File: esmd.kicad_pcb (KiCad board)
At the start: 2 copper layers, 25.9 x 63 mm, 21 parts, among them J1 Conn_01x04, J2 Conn_01x08, J3 Conn_01x04, J4 Conn_01x08, J5 Conn_01x04, J6 Conn_01x08, J7 Conn_01x02, J8 Conn_01x02, U1 74HC245, U2 74HC245, U3 LM78M05_TO252

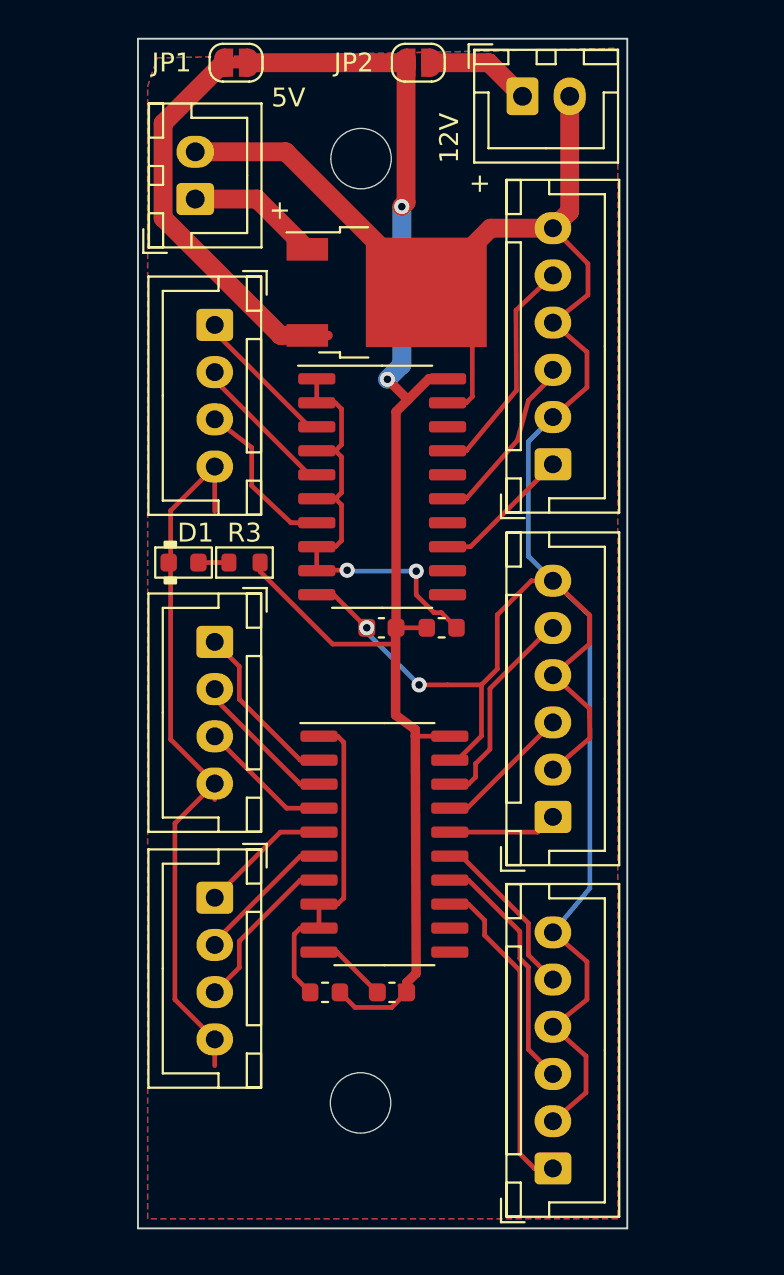
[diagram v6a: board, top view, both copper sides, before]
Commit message: Add alternate footprints.
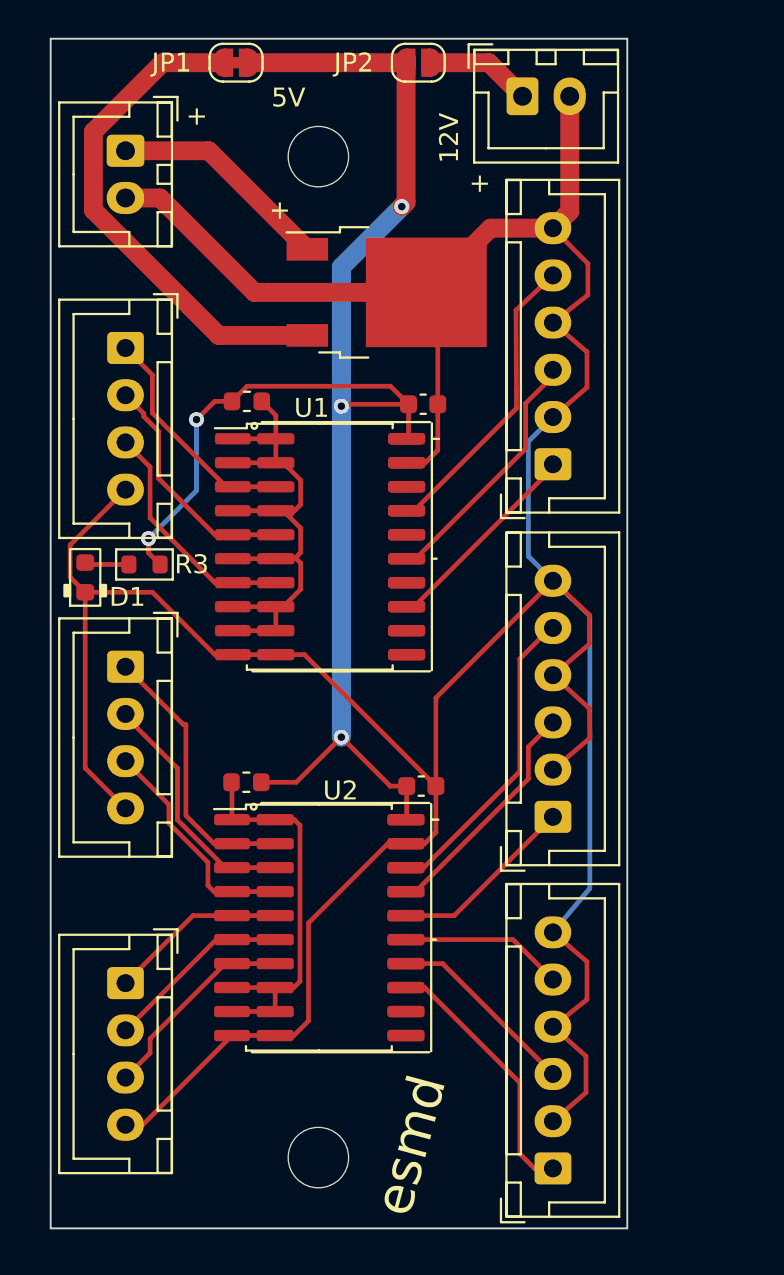
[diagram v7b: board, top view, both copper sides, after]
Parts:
- added U1A1: 74HC245, Package_SO:SOP-20_7.5x12.8mm_P1.27mm, F.Cu at (165.1, 106.7)
- added U2A1: 74HC245, Package_SO:SOP-20_7.5x12.8mm_P1.27mm, F.Cu at (165.0, 126.8)
- U1, U2: footprint Package_SO:SO-20_5.3x12.6mm_P1.27mm -> PCM_Package_SO_AKL:SO-20_5.3x12.6mm_P1.27mm
- moved R1 15.8 mm to (161.2, 99.0)
- moved C1 12.0 mm to (170.5, 99.1), turned to 0 degrees
- moved R2 11.9 mm to (161.2, 119.1)
- moved C2 11.0 mm to (170.4, 119.3), turned to 0 degrees
- moved J5 6.54 mm to (154.8, 129.8)
- moved R3 5.30 mm to (155.8, 107.6)
- moved D1 5.27 mm to (152.7, 108.3), turned to 90 degrees
- moved U2 4.99 mm to (166.2, 126.8)
- moved J3 4.90 mm to (154.8, 113.0)
- moved J1 4.88 mm to (154.8, 96.1)
- moved J7 4.49 mm to (154.8, 85.7), turned to -90 degrees
- moved U1 3.84 mm to (166.2, 106.7)
- moved H2 3.66 mm to (165.0, 139.0)
- moved H1 2.26 mm to (165.0, 86.0)
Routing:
- net GND: track 174.9 -> 201.3 mm, vias 2 -> 0
- net Net-(U1-A->B): track 24.3 -> 31.8 mm, vias 2 -> 0
- net Net-(JP1-B): track 20.9 -> 26.6 mm
- net Enable_out2: track 11.2 -> 16.7 mm
- net Step_out2: track 7.34 -> 12.5 mm
- net Step2: track 7.90 -> 13.0 mm
- net Dir2: track 7.10 -> 12.1 mm
- net Net-(J7-Pin_1): track 7.04 -> 11.8 mm
- net Step1: track 7.90 -> 12.6 mm
- net Enable2: track 10.00 -> 14.6 mm
- net +5V: track 79.4 -> 83.8 mm, vias 2 -> 5
- net Enable1: track 7.86 -> 12.2 mm
- net Dir_out2: track 5.80 -> 9.95 mm
- net Step_out1: track 9.45 -> 13.5 mm
- net Net-(U2-A->B): track 17.3 -> 21.3 mm
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- removed copper zone on B.Cu, net GND
- removed copper zone on F.Cu, net GND
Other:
- board size 25.9 x 63 mm -> 30.5 x 63 mm
- board text added: "esmd"
